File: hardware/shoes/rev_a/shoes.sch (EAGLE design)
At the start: 36 parts, among them J4 TC2030-JLINK-NL, Q1 MOSFET-NCHANNELXFDN-3, Q2 MOSFET-NCHANNELXFDN-3, Q3 MOSFET-NCHANNELXFDN-3, Q4 MOSFET-NCHANNELXFDN-3, U1 NRF51822QF, U2 ADXL362, X1 16MHz

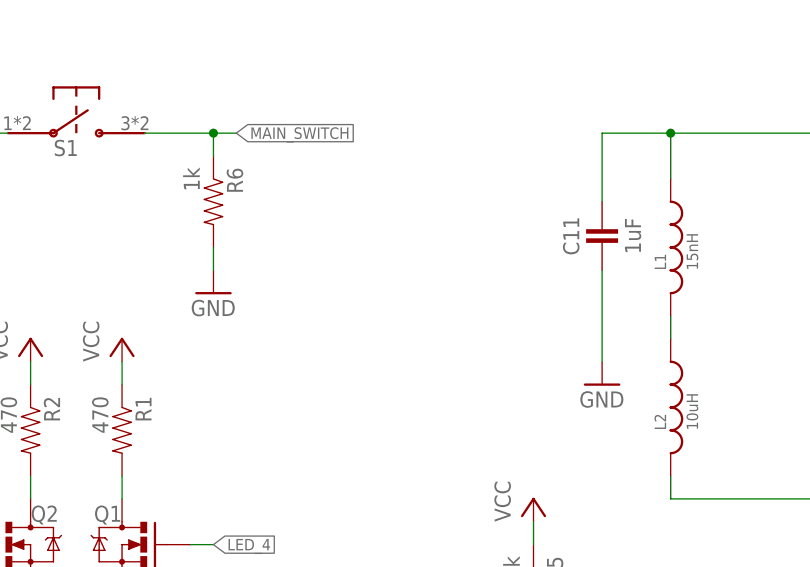
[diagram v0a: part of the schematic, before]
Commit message: board changes
added cap from power to ground
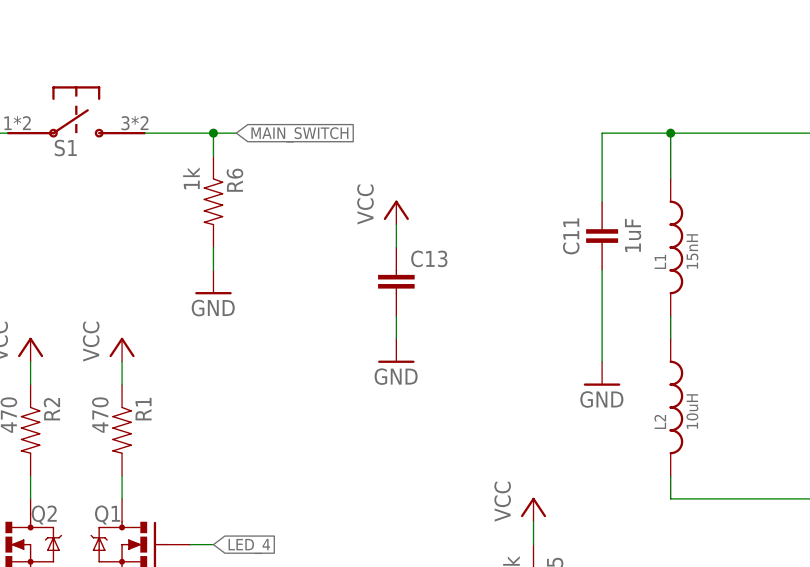
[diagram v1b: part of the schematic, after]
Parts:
- added C13: (no value), SparkFun-Capacitors:CAP0805
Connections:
- net GND: now also C13.2
- net VCC: now also C13.1
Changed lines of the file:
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@@
 <part name="GND9" library="supply1" deviceset="GND" device=""/>
 <part name="LOGO3" library="logos" deviceset="UMICH_SOLID" device="_TINY"/>
+<part name="C13" library="SparkFun-Capacitors" deviceset="CAP" device="0805"/>
+<part name="P+10" library="supply1" deviceset="VCC" device=""/>
+<part name="GND15" library="supply1" deviceset="GND" device=""/>
 </parts>
 <sheets>
@@
 <instance part="GND9" gate="1" x="91.44" y="33.02"/>
 <instance part="LOGO3" gate="G$1" x="231.14" y="172.72"/>
+<instance part="C13" gate="G$1" x="66.04" y="149.86"/>
+<instance part="P+10" gate="VCC" x="66.04" y="160.02"/>
+<instance part="GND15" gate="1" x="66.04" y="142.24"/>
 </instances>
 <busses>
@@
 <wire x1="91.44" y1="38.1" x2="91.44" y2="35.56" width="0.1524" layer="91"/>
 <pinref part="GND9" gate="1" pin="GND"/>
+</segment>
+<segment>
+<pinref part="GND15" gate="1" pin="GND"/>
+<pinref part="C13" gate="G$1" pin="2"/>
+<wire x1="66.04" y1="144.78" x2="66.04" y2="147.32" width="0.1524" layer="91"/>
 </segment>
 </net>
@@
 <junction x="86.36" y="48.26"/>
 </segment>
+<segment>
+<pinref part="C13" gate="G$1" pin="1"/>
+<pinref part="P+10" gate="VCC" pin="VCC"/>
+<wire x1="66.04" y1="154.94" x2="66.04" y2="157.48" width="0.1524" layer="91"/>
+</segment>
 </net>

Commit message: update pcb
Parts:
- added BAT1: BAT-CON-112TR, batteries:BAT-CON-112TR
- added TP1, TP2: TEST_POINT_0.020IN, headers:TEST_POINT_0.020IN
- added TP3, TP4, TP5, TP6, TP7: TPSQTP06SQ, testpad:TPSQTP06SQ
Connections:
- new net N$1: TP2.TESTPOINT, U1.P17
- net !ACCEL_CS: now also TP4.TP
- net ACCEL_INT: now also TP3.TP
- net GND: now also BAT1.-, TP1.TESTPOINT
- net MISO: now also TP6.TP
- net MOSI: now also TP7.TP
- net SCLK: now also TP5.TP
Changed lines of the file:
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@@
 <layer number="56" name="wert" color="7" fill="1" visible="no" active="no"/>
 <layer number="57" name="tCAD" color="7" fill="1" visible="no" active="no"/>
+<layer number="59" name="Invisible" color="7" fill="1" visible="no" active="no"/>
+<layer number="61" name="stand" color="7" fill="1" visible="no" active="no"/>
 <layer number="90" name="Modules" color="5" fill="1" visible="yes" active="yes"/>
 <layer number="91" name="Nets" color="2" fill="1" visible="yes" active="yes"/>
@@
 <layer number="127" name="_tValues" color="7" fill="1" visible="yes" active="yes"/>
 <layer number="128" name="_bValues" color="7" fill="1" visible="yes" active="yes"/>
+<layer number="130" name="bLogo" color="7" fill="1" visible="yes" active="yes"/>
 <layer number="131" name="tAdjust" color="7" fill="1" visible="yes" active="yes"/>
 <layer number="132" name="bAdjust" color="7" fill="1" visible="yes" active="yes"/>
@@
 <layer number="223" name="223bmp" color="24" fill="1" visible="no" active="no"/>
 <layer number="224" name="224bmp" color="25" fill="1" visible="no" active="no"/>
+<layer number="231" name="Eagle3D_PG1" color="14" fill="1" visible="yes" active="yes"/>
+<layer number="232" name="Eagle3D_PG2" color="14" fill="2" visible="yes" active="yes"/>
+<layer number="233" name="Eagle3D_PG3" color="14" fill="4" visible="yes" active="yes"/>
 <layer number="248" name="Housing" color="7" fill="1" visible="yes" active="yes"/>
 <layer number="249" name="Edge" color="7" fill="1" visible="yes" active="yes"/>
@@
 <part name="P+10" library="supply1" deviceset="VCC" device=""/>
 <part name="GND15" library="supply1" deviceset="GND" device=""/>
+<part name="BAT1" library="batteries" deviceset="BAT-CON-112TR" device=""/>
+<part name="GND16" library="supply1" deviceset="GND" device=""/>
+<part name="TP2" library="headers" deviceset="TEST_POINT_0.020IN" device=""/>
+<part name="TP1" library="headers" deviceset="TEST_POINT_0.020IN" device=""/>
+<part name="TP3" library="testpad" deviceset="TPSQ" device="TP06SQ"/>
+<part name="TP4" library="testpad" deviceset="TPSQ" device="TP06SQ"/>
+<part name="TP5" library="testpad" deviceset="TPSQ" device="TP06SQ"/>
+<part name="TP6" library="testpad" deviceset="TPSQ" device="TP06SQ"/>
+<part name="TP7" library="testpad" deviceset="TPSQ" device="TP06SQ"/>
 </parts>
 <sheets>
@@
 <instance part="P+10" gate="VCC" x="66.04" y="160.02"/>
 <instance part="GND15" gate="1" x="66.04" y="142.24"/>
+<instance part="BAT1" gate="G$1" x="20.32" y="25.4"/>
+<instance part="GND16" gate="1" x="27.94" y="15.24"/>
+<instance part="TP2" gate="G$1" x="172.72" y="119.38" rot="R90"/>
+<instance part="TP1" gate="G$1" x="27.94" y="27.94" rot="R270"/>
+<instance part="TP3" gate="G$1" x="66.04" y="25.4" rot="R180"/>
+<instance part="TP4" gate="G$1" x="101.6" y="17.78" rot="R180"/>
+<instance part="TP5" gate="G$1" x="104.14" y="22.86" rot="R180"/>
+<instance part="TP6" gate="G$1" x="106.68" y="25.4" rot="R180"/>
+<instance part="TP7" gate="G$1" x="109.22" y="27.94" rot="R180"/>
 </instances>
 <busses>
@@
 <pinref part="C13" gate="G$1" pin="2"/>
 <wire x1="66.04" y1="144.78" x2="66.04" y2="147.32" width="0.1524" layer="91"/>
+</segment>
+<segment>
+<pinref part="BAT1" gate="G$1" pin="-"/>
+<wire x1="25.4" y1="25.4" x2="27.94" y2="25.4" width="0.1524" layer="91"/>
+<wire x1="27.94" y1="25.4" x2="27.94" y2="17.78" width="0.1524" layer="91"/>
+<pinref part="GND16" gate="1" pin="GND"/>
+<pinref part="TP1" gate="G$1" pin="TESTPOINT"/>
+<junction x="27.94" y="25.4"/>
 </segment>
 </net>
@@
 <segment>
 <pinref part="U2" gate="G$1" pin="MOSI"/>
-<wire x1="101.6" y1="25.4" x2="99.06" y2="25.4" width="0.1524" layer="91"/>
-<label x="101.6" y="25.4" size="1.27" layer="95" xref="yes"/>
+<wire x1="109.22" y1="25.4" x2="99.06" y2="25.4" width="0.1524" layer="91"/>
+<label x="109.22" y="25.4" size="1.27" layer="95" xref="yes"/>
+<pinref part="TP7" gate="G$1" pin="TP"/>
 </segment>
 <segment>
@@
 <segment>
 <pinref part="U2" gate="G$1" pin="MISO"/>
-<wire x1="101.6" y1="22.86" x2="99.06" y2="22.86" width="0.1524" layer="91"/>
-<label x="101.6" y="22.86" size="1.27" layer="95" xref="yes"/>
+<wire x1="106.68" y1="22.86" x2="99.06" y2="22.86" width="0.1524" layer="91"/>
+<label x="106.68" y="22.86" size="1.27" layer="95" xref="yes"/>
+<pinref part="TP6" gate="G$1" pin="TP"/>
 </segment>
 <segment>
@@
 <segment>
 <pinref part="U2" gate="G$1" pin="SCLK"/>
-<wire x1="101.6" y1="20.32" x2="99.06" y2="20.32" width="0.1524" layer="91"/>
-<label x="101.6" y="20.32" size="1.27" layer="95" xref="yes"/>
+<wire x1="104.14" y1="20.32" x2="99.06" y2="20.32" width="0.1524" layer="91"/>
+<label x="104.14" y="20.32" size="1.27" layer="95" xref="yes"/>
+<pinref part="TP5" gate="G$1" pin="TP"/>
 </segment>
 <segment>
@@
 <wire x1="101.6" y1="15.24" x2="99.06" y2="15.24" width="0.1524" layer="91"/>
 <label x="101.6" y="15.24" size="1.27" layer="95" xref="yes"/>
+<pinref part="TP4" gate="G$1" pin="TP"/>
 </segment>
 <segment>
@@
 <wire x1="68.58" y1="22.86" x2="66.04" y2="22.86" width="0.1524" layer="91"/>
 <label x="66.04" y="22.86" size="1.27" layer="95" rot="R180" xref="yes"/>
+<pinref part="TP3" gate="G$1" pin="TP"/>
 </segment>
 <segment>
@@
 </segment>
 </net>
+<net name="N$1" class="0">
+<segment>
+<pinref part="U1" gate="G$1" pin="P17"/>
+<pinref part="TP2" gate="G$1" pin="TESTPOINT"/>
+<wire x1="160.02" y1="124.46" x2="172.72" y2="124.46" width="0.1524" layer="91"/>
+<wire x1="172.72" y1="124.46" x2="172.72" y2="121.92" width="0.1524" layer="91"/>
+</segment>
+</net>
